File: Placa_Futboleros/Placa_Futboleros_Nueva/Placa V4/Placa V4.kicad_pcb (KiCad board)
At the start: 2 copper layers, 100 x 70 mm, 30 parts, among them J1 LiPo, J2 MI_Ad, J3 MI_At, J4 MD_Ad, J5 MD_At, J6 Pilas, U1 ESP32_30p, U2 DRV8833, U3 DRV8833, U5 INA219AxD

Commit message: Correcciones menores de la placa V4
Sobre espacio entre pistas, entre otros.
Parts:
- added C1: 100nF, Capacitor_THT:C_Disc_D10.0mm_W2.5mm_P5.00mm, F.Cu at (94.6, 94.2)
- moved D4 5.30 mm to (50.6, 61.2)
- moved R3 2.13 mm to (93.0, 90.1)
- moved D1 1.78 mm to (133.9, 71.1)
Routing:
- net VCC: track 293.5 -> 300.5 mm
- net Net-(D4-A): track 13.5 -> 9.09 mm
- net GND: track 344.4 -> 348.7 mm
- net 5V: track 51.9 -> 48.2 mm
- net /ADC: track 110.7 -> 107.9 mm
- net Net-(D1-K): track 29.1 -> 27.3 mm
- net Net-(D1-A): track 26.4 -> 25.0 mm
- net SLEEP_M2: track 35.7 -> 34.9 mm
- net 3V3: track 148.0 -> 147.4 mm

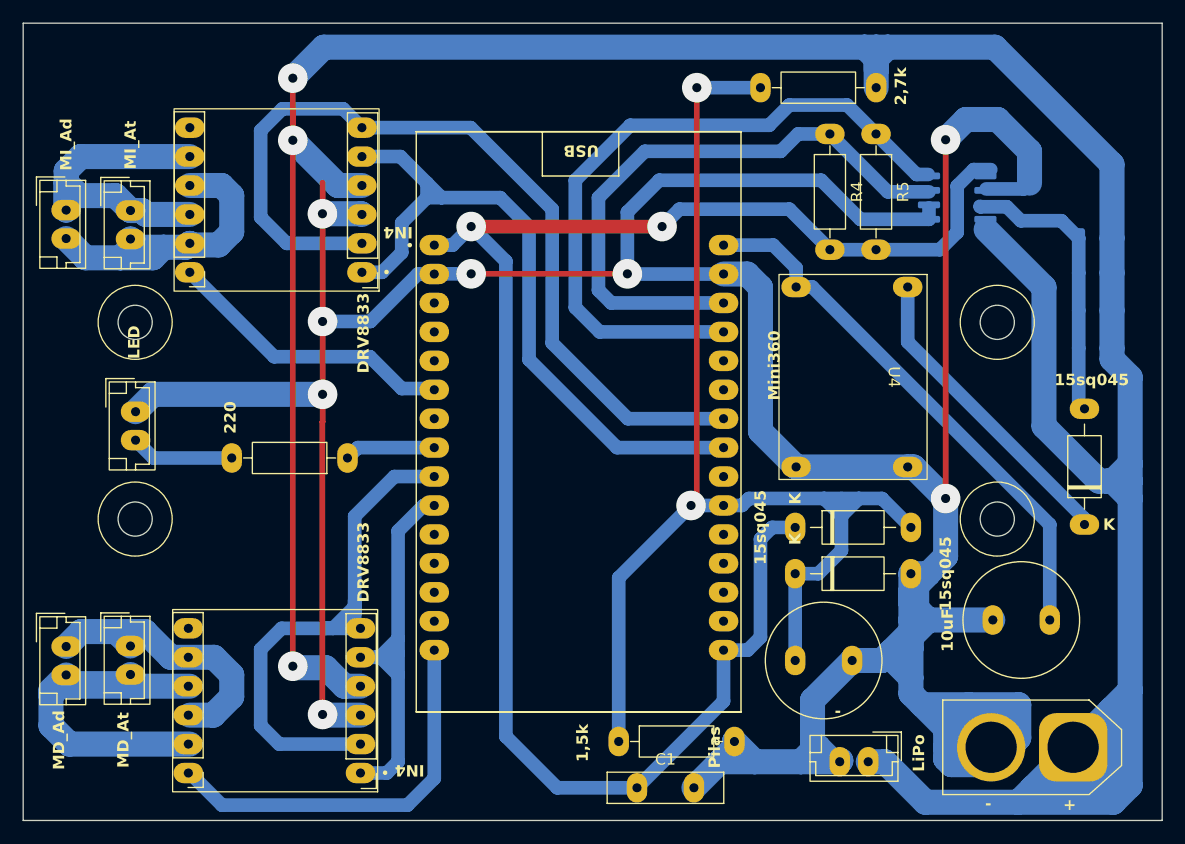
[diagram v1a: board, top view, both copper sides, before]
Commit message: Actualización placa V4
Se reordenan pistas, se repiensa resistencias smd para x4 de 0,47 ohm
y se deja más prolija. (Chequeado con Dominici)
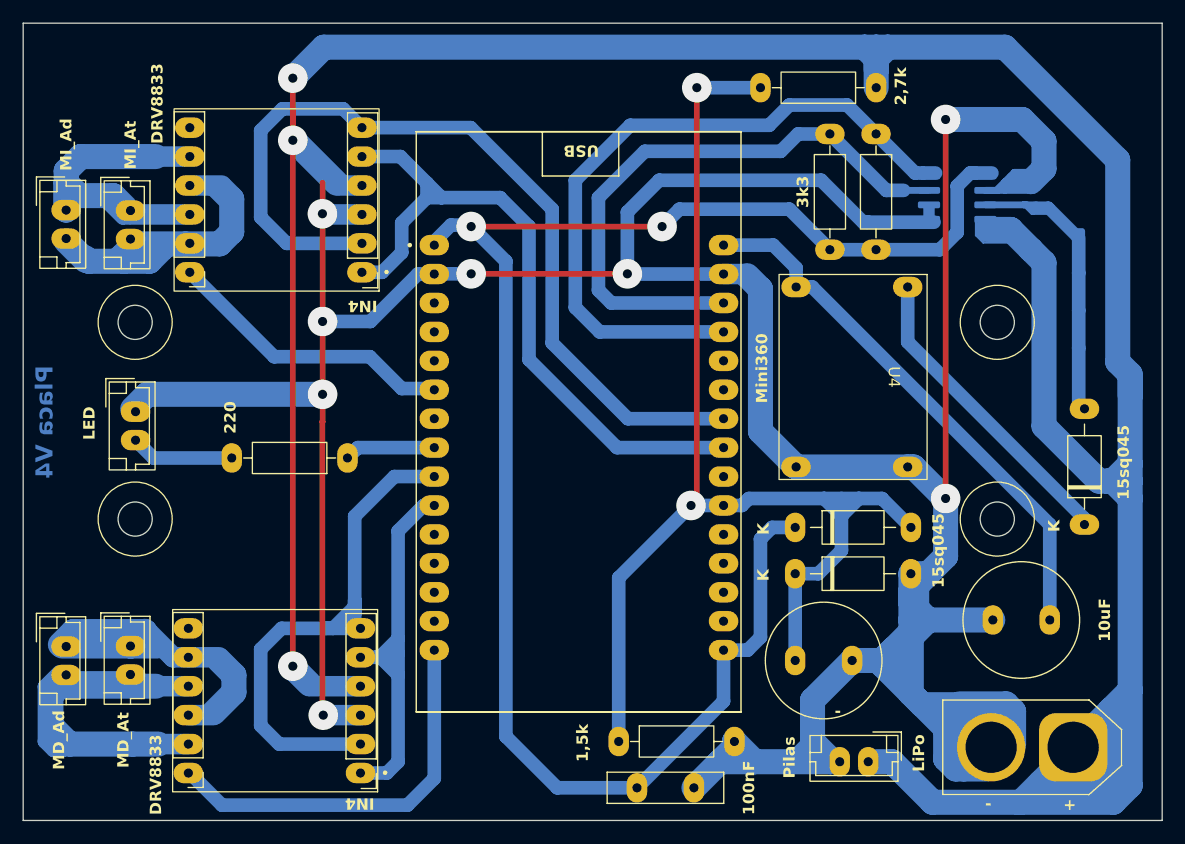
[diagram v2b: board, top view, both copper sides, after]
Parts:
- R10, R7, R8, R9: value 0,22 -> 0,47
- U5: value INA219AxD -> INA219
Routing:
- net GND: track 348.7 -> 366.4 mm
- net VCC: track 300.5 -> 316.0 mm
- net Net-(J4-Pin_1): track 24.7 -> 35.1 mm
- net Net-(J4-Pin_2): track 38.3 -> 48.5 mm
- net Net-(J2-Pin_1): track 29.2 -> 32.0 mm
- net Net-(D1-A): track 25.0 -> 27.6 mm
- net Net-(J2-Pin_2): track 29.1 -> 31.2 mm
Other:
- board text added: "Placa V4"

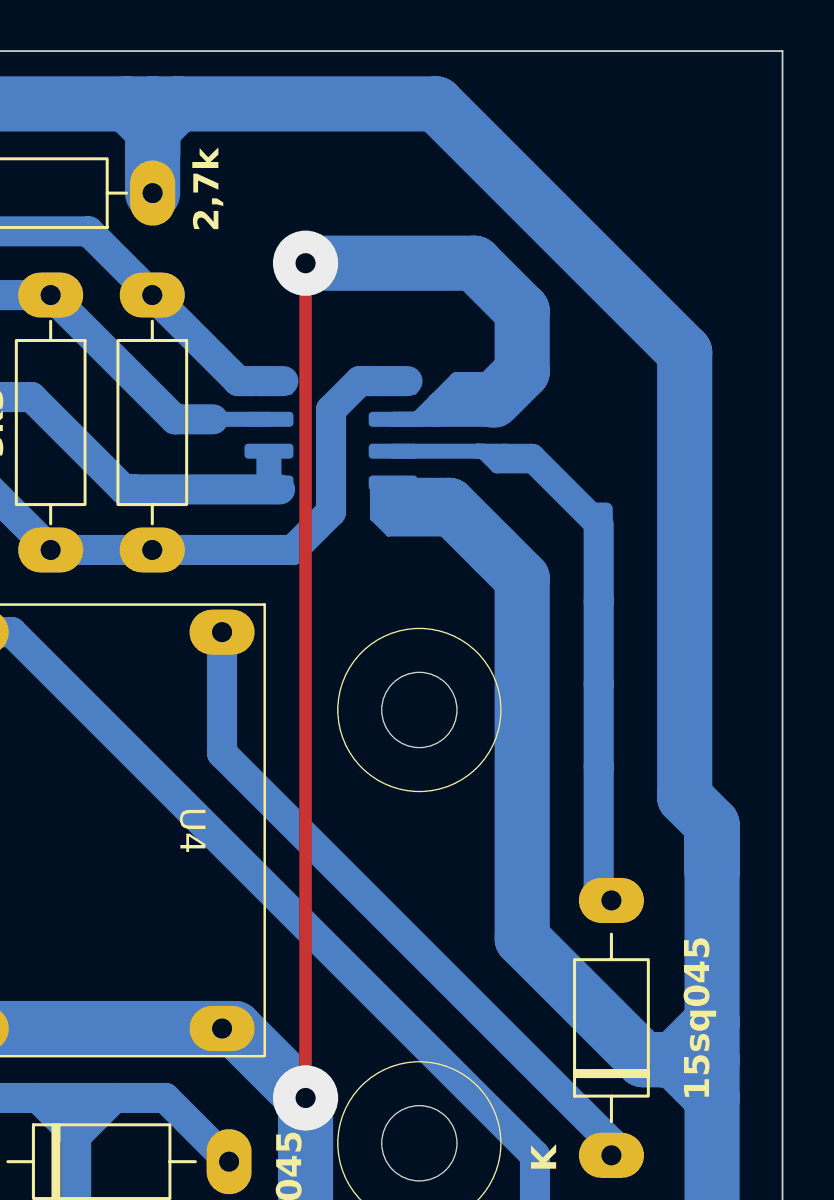
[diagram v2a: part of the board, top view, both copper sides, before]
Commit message: \Pequeño cambio encapsulado 2516 R_smd
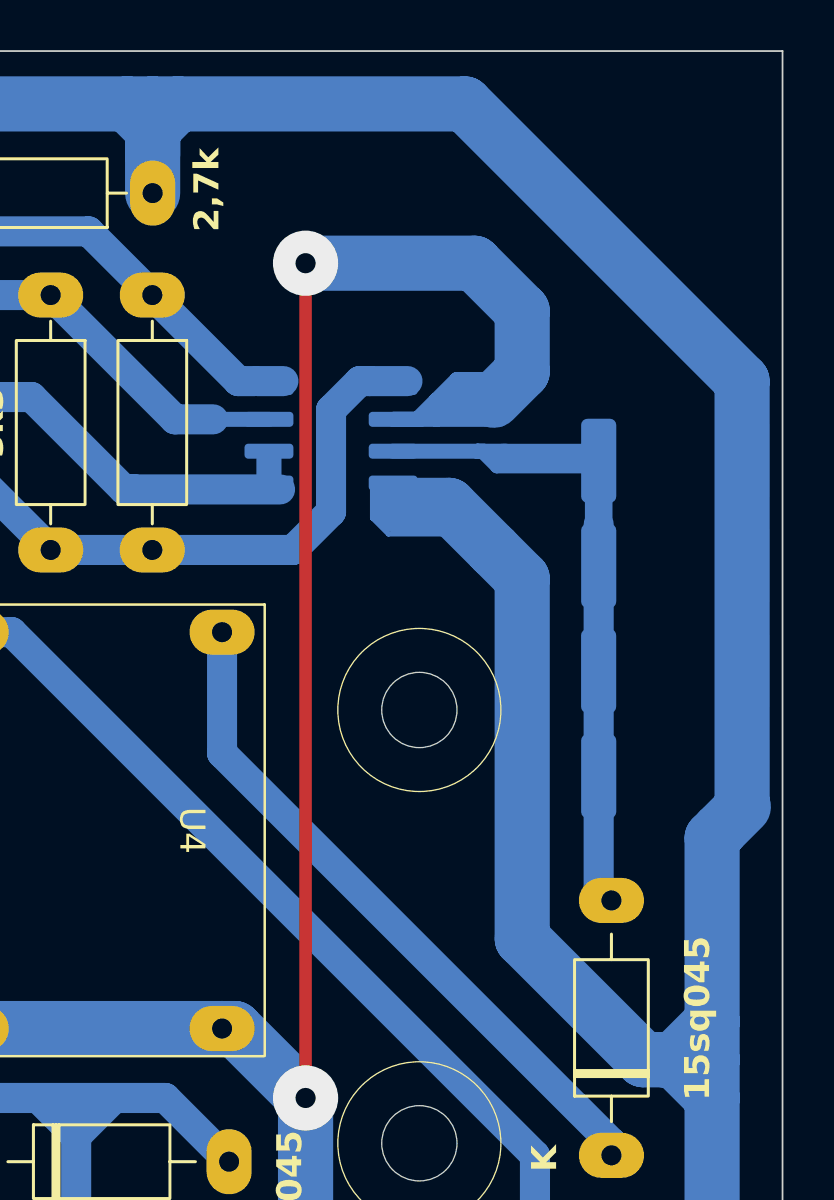
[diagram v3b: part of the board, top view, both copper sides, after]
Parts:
- R10, R7, R8, R9: footprint Resistor_SMD:R_1206_3216Metric -> Resistor_SMD:R_2512_6332Metric_Pad1.40x3.35mm_HandSolder
- U5: value INA219 -> INA219AxD
- moved R7 3.00 mm to (136.4, 43.4)
- moved R8 2.11 mm to (136.4, 47.6)
- moved R9 1.67 mm to (136.4, 51.8)
- moved R10 1.63 mm to (136.4, 56.0)
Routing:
- net Net-(D1-A): track 27.6 -> 31.3 mm
